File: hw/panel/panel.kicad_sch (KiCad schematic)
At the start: 37 parts, among them J1 Barrel_Jack, J2 Conn_ST_STDC14, Q1 BS170F, U1 STM32G031K8Tx, U2 RFM69HW, U3 AMS1117-3.3, U4 MCP16301Hx-xCH, Y1 32.768KHz

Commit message: panel
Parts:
- removed AE1: Antenna, RF_Antenna:NiceRF_SW868-TH13_868Mhz, symbol Device:Antenna
- removed C21, C23, C24, C25: 10uF, Capacitor_SMD:C_1206_3216Metric_Pad1.33x1.80mm_HandSolder, symbol Device:C
- removed C22: C, Capacitor_SMD:C_0805_2012Metric_Pad1.18x1.45mm_HandSolder, symbol Device:C
- removed D26: 1N4148W, Diode_SMD:D_SOD-123, symbol Diode:1N4148W
- removed D27: B140-E3, Diode_SMD:D_SMA, symbol Diode:B140-E3
- removed L1: 22uH, Inductor_SMD:L_Coilcraft_LPS4018, symbol Device:L
- removed R4: 52.3k, Resistor_SMD:R_0805_2012Metric_Pad1.20x1.40mm_HandSolder, symbol Device:R
- removed R5: 10k, Resistor_SMD:R_0805_2012Metric_Pad1.20x1.40mm_HandSolder, symbol Device:R
- removed U4: MCP16301Hx-xCH, Package_TO_SOT_SMD:SOT-23-6, symbol Regulator_Switching:MCP16301Hx-xCH
- added C11, C9: 100nF, Capacitor_SMD:C_0805_2012Metric_Pad1.18x1.45mm_HandSolder, symbol Device:C
- added C8: 4.7uF, Capacitor_SMD:C_0805_2012Metric_Pad1.18x1.45mm_HandSolder, symbol Device:C
- added J2: Conn_Coaxial, Connector_Coaxial:SMA_Amphenol_901-143_Horizontal, symbol Connector:Conn_Coaxial
- added J4: Conn_01x04_Socket, Connector_PinSocket_2.54mm:PinSocket_1x04_P2.54mm_Horizontal, symbol Connector:Conn_01x04_Socket
- added J5: Conn_01x04_Pin, Connector_PinHeader_2.54mm:PinHeader_1x04_P2.54mm_Horizontal, symbol Connector:Conn_01x04_Pin
- J1: footprint Connector_BarrelJack:BarrelJack_CUI_PJ-063AH_Horizontal -> Connector_AMASS:AMASS_XT30PW-M_1x02_P2.50mm_Horizontal
- renumbered C20 to C10, C19 to C7, H3 to H2, H2 to H3, J2 to J3, JP2 to JP1, JP26 to JP2, R2 to R1, R1 to R2, U3 to U2, U2 to U3
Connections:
- net +5V is gone; now on net +6V: C7.1, R3.1, U2.3 (VI)
- net +3V3: now also C11.1, C8.1, C9.1
- net GND: now also C11.2, C8.2, C9.2, J2.2 (Ext), J4.1 (Pin_1), J5.1 (Pin_1)
- net leds/RGB_IN: now also J5.3 (Pin_3)
- net leds/RGB_OUT: now also J4.3 (Pin_3)
- net leds1/RGB_IN: now also J4.2 (Pin_2)
- net leds1/RGB_OUT: now also J5.2 (Pin_2)
- net +6V: now reaches J1.1
- net +6V: now also J4.4 (Pin_4), J5.4 (Pin_4)
- net at U3.10 (ANA): now also J2.1 (In)
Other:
- moved on the sheet: C10, C7, J3, JP2, U2

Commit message: panel progress
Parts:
- J1: footprint Connector_AMASS:AMASS_XT30PW-M_1x02_P2.50mm_Horizontal -> Connector_Molex:Molex_Micro-Fit_3.0_43650-0200_1x02_P3.00mm_Horizontal
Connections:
- net +3V3: now also D1.2 (A); no longer R1.1
- net at U1.20 (PC6): now also R1.2; no longer D1.1 (K)
- new net: D1.1 (K), R1.1
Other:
- moved on the sheet: D1, R1

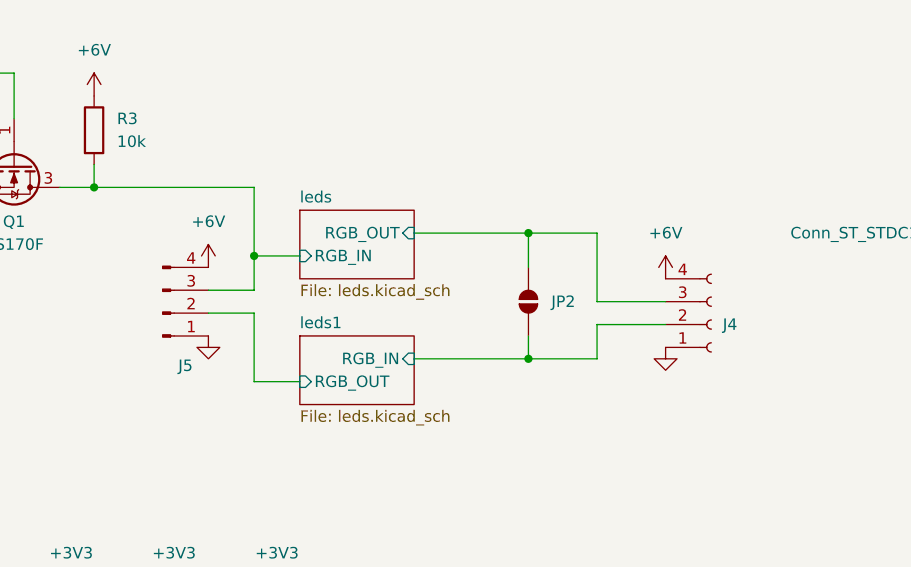
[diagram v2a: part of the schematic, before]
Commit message: extend top to 200mm
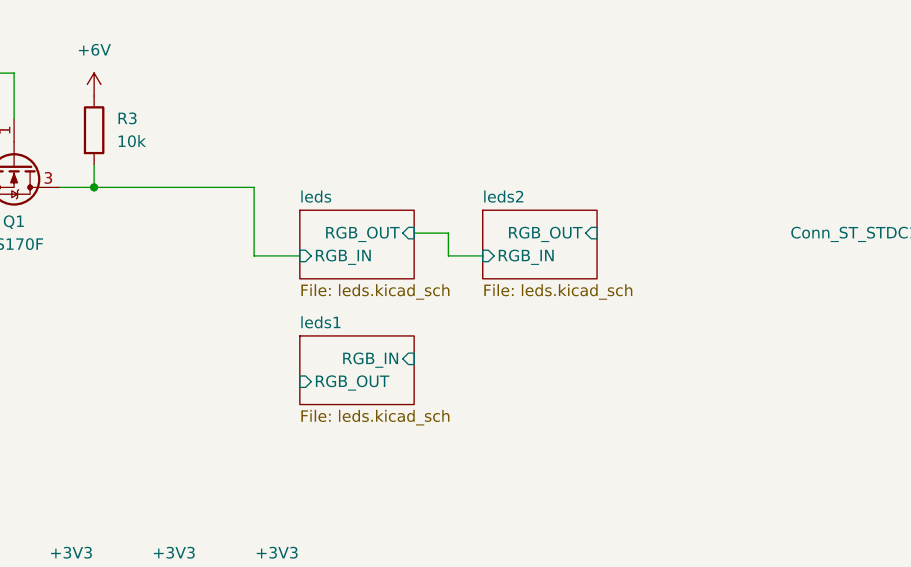
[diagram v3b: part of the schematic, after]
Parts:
- removed J4: Conn_01x04_Socket, Connector_PinSocket_2.54mm:PinSocket_1x04_P2.54mm_Horizontal, symbol Connector:Conn_01x04_Socket
- removed J5: Conn_01x04_Pin, Connector_PinHeader_2.54mm:PinHeader_1x04_P2.54mm_Horizontal, symbol Connector:Conn_01x04_Pin
- removed JP2: SolderJumper_2_Bridged, Jumper:SolderJumper-2_P1.3mm_Open_TrianglePad1.0x1.5mm, symbol Jumper:SolderJumper_2_Open
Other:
- added sheet leds2 (leds.kicad_sch)

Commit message: bot left
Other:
- sheet leds renamed led_top_left
- sheet leds1 renamed led_bot_left
- sheet leds2 renamed led_top_right
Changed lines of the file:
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@@
 			(color 0 0 0 0.0000)
 		)
-		(property "Sheetname" "leds"
+		(property "Sheetname" "led_top_left"
 			(at 173.99 60.2484 0)
 			(effects
@@
 			(color 0 0 0 0.0000)
 		)
-		(property "Sheetname" "leds1"
+		(property "Sheetname" "led_bot_left"
 			(at 173.99 74.2184 0)
 			(effects
@@
 			(project "panel"
 				(path "/75e15db9-5774-4cb3-bd4e-28bd152fa038"
-					(page "3")
+					(page "5")
 				)
 			)
@@
 			(color 0 0 0 0.0000)
 		)
-		(property "Sheetname" "leds2"
+		(property "Sheetname" "led_top_right"
 			(at 194.31 60.2484 0)
 			(effects
@@
 			(project "panel"
 				(path "/75e15db9-5774-4cb3-bd4e-28bd152fa038"
-					(page "4")
+					(page "3")
 				)
 			)

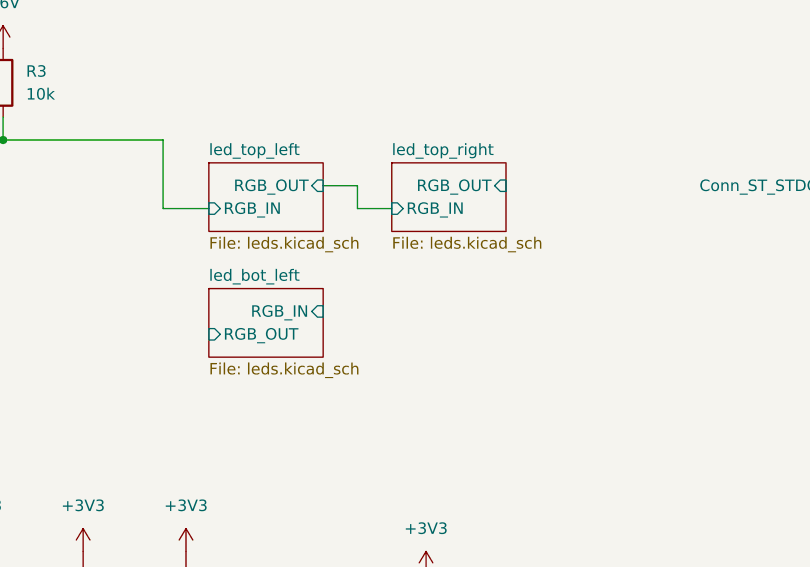
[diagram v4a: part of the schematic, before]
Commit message: Added bot right
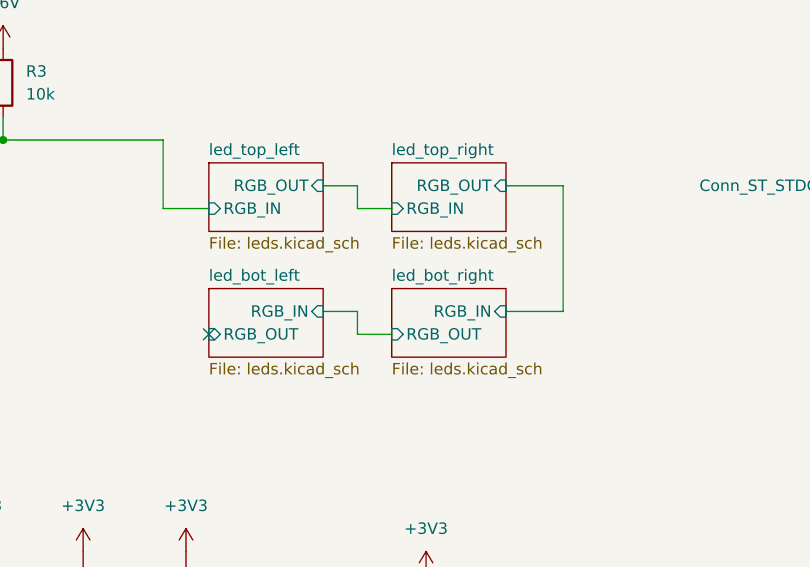
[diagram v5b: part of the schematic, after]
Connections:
- no-connect marks 23 -> 24
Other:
- added sheet led_bot_right (leds.kicad_sch)
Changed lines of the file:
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@@
 	)
 	(no_connect
+		(at 173.99 80.01)
+	)
+	(no_connect
 		(at 210.82 119.38)
 	)
@@
 	(wire
 		(pts
+			(xy 190.5 80.01) (xy 190.5 77.47)
+		)
+		(stroke
+			(width 0)
+			(type default)
+		)
+	)
+	(wire
+		(pts
 			(xy 72.39 38.1) (xy 76.2 38.1)
 		)
@@
 	(wire
 		(pts
+			(xy 194.31 80.01) (xy 190.5 80.01)
+		)
+		(stroke
+			(width 0)
+			(type default)
+		)
+	)
+	(wire
+		(pts
 			(xy 210.82 111.76) (xy 217.17 111.76)
 		)
@@
 	(wire
 		(pts
+			(xy 213.36 77.47) (xy 207.01 77.47)
+		)
+		(stroke
+			(width 0)
+			(type default)
+		)
+	)
+	(wire
+		(pts
 			(xy 102.87 149.86) (xy 102.87 147.32)
 		)
@@
 	(wire
 		(pts
+			(xy 186.69 77.47) (xy 190.5 77.47)
+		)
+		(stroke
+			(width 0)
+			(type default)
+		)
+	)
+	(wire
+		(pts
 			(xy 167.64 124.46) (xy 170.18 124.46)
 		)
@@
 	(wire
 		(pts
+			(xy 213.36 63.5) (xy 213.36 77.47)
+		)
+		(stroke
+			(width 0)
+			(type default)
+		)
+	)
+	(wire
+		(pts
 			(xy 127 151.13) (xy 127 149.86)
 		)
@@
 	(wire
 		(pts
+			(xy 207.01 63.5) (xy 213.36 63.5)
+		)
+		(stroke
+			(width 0)
+			(type default)
+		)
+	)
+	(wire
+		(pts
 			(xy 55.88 48.26) (xy 55.88 50.8)
 		)
@@
 				)
 			)
+		)
+	)
+	(sheet
+		(at 194.31 74.93)
+		(size 12.7 7.62)
+		(fields_autoplaced yes)
+		(stroke
+			(width 0.1524)
+			(type solid)
+		)
+		(fill
+			(color 0 0 0 0.0000)
+		)
+		(property "Sheetname" "led_bot_right"
+			(at 194.31 74.2184 0)
+			(effects
+				(font
+					(size 1.27 1.27)
+				)
+				(justify left bottom)
+			)
+		)
+		(property "Sheetfile" "leds.kicad_sch"
+			(at 194.31 83.1346 0)
+			(effects
+				(font
+					(size 1.27 1.27)
+				)
+				(justify left top)
+			)
+		)
+		(pin "RGB_IN" input
+			(at 207.01 77.47 0)
+			(effects
+				(font
+					(size 1.27 1.27)
+				)
+				(justify right)
+			)
+		)
+		(pin "RGB_OUT" input
+			(at 194.31 80.01 180)
+			(effects
+				(font
+					(size 1.27 1.27)
+				)
+				(justify left)
+			)
+		)
+		(instances
+			(project "panel"
+				(path "/75e15db9-5774-4cb3-bd4e-28bd152fa038"
+					(page "4")
+				)
+			)

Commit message: holes
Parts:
- added H200, H201: MountingHole, MountingHole:MountingHole_3.2mm_M3, symbol Mechanical:MountingHole
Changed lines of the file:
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@@
+	)
+	(symbol
+		(lib_id "Mechanical:MountingHole")
+		(at 257.81 22.86 0)
+		(unit 1)
+		(exclude_from_sim yes)
+		(in_bom no)
+		(on_board yes)
+		(dnp no)
+		(fields_autoplaced yes)
+		(property "Reference" "H200"
+			(at 260.35 21.5899 0)
+			(effects
+				(font
+					(size 1.27 1.27)
+				)
+				(justify left)
+				(hide yes)
+			)
+		)
+		(property "Value" "MountingHole"
+			(at 260.35 24.1299 0)
+			(effects
+				(font
+					(size 1.27 1.27)
+				)
+				(justify left)
+				(hide yes)
+			)
+		)
+		(property "Footprint" "MountingHole:MountingHole_3.2mm_M3"
+			(at 257.81 22.86 0)
+			(effects
+				(font
+					(size 1.27 1.27)
+				)
+				(hide yes)
+			)
+		)
+		(property "Datasheet" "~"
+			(at 257.81 22.86 0)
+			(effects
+				(font
+					(size 1.27 1.27)
+				)
+				(hide yes)
+			)
+		)
+		(property "Description" "Mounting Hole without connection"
+			(at 257.81 22.86 0)
+			(effects
+				(font
+					(size 1.27 1.27)
+				)
+				(hide yes)
+			)
+		)
+		(instances
+			(project "panel"
+				(path "/75e15db9-5774-4cb3-bd4e-28bd152fa038"
+					(reference "H200")
+					(unit 1)
+				)
+			)
+		)
 	)
 	(symbol
@@
 					(unit 1)
 				)
+			)
+		)
+	)
+	(symbol
+		(lib_id "Mechanical:MountingHole")
+		(at 257.81 26.67 0)
+		(unit 1)
+		(exclude_from_sim yes)
+		(in_bom no)
+		(on_board yes)
+		(dnp no)
+		(fields_autoplaced yes)
+		(property "Reference" "H201"
+			(at 260.35 25.3999 0)
+			(effects
+				(font
+					(size 1.27 1.27)
+				)
+				(justify left)
+				(hide yes)
+			)
+		)
+		(property "Value" "MountingHole"
+			(at 260.35 27.9399 0)
+			(effects
+				(font
+					(size 1.27 1.27)
+				)
+				(justify left)
+				(hide yes)
+			)
+		)
+		(property "Footprint" "MountingHole:MountingHole_3.2mm_M3"
+			(at 257.81 26.67 0)
+			(effects
+				(font
+					(size 1.27 1.27)
+				)
+				(hide yes)
+			)
+		)
+		(property "Datasheet" "~"
+			(at 257.81 26.67 0)
+			(effects
+				(font
+					(size 1.27 1.27)
+				)
+				(hide yes)
+			)
+		)
+		(property "Description" "Mounting Hole without connection"
+			(at 257.81 26.67 0)
+			(effects
+				(font
+					(size 1.27 1.27)
+				)
+				(hide yes)
+			)
+		)
+		(instances
+			(project "panel"
+				(path "/75e15db9-5774-4cb3-bd4e-28bd152fa038"
+					(reference "H201")
+					(unit 1)
+				)

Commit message: x
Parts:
- removed D1: LED, LED_SMD:LED_0805_2012Metric_Pad1.15x1.40mm_HandSolder, symbol Device:LED
- added D1: ~, panel:light_guide, symbol panel:LED_ARRAY_4
- added R4, R5, R6: 680, Resistor_SMD:R_0805_2012Metric_Pad1.20x1.40mm_HandSolder, symbol Device:R
- R1: value 100k -> 680
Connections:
- net +3V3: now also R1.2
- net GND: now also D1.1 (K), D1.3 (K), D1.5 (K), D1.7 (K)
- net LED_TX: now reaches U1.11 (PA4)
- net LED_TX: now also R4.2
- net LED_RX: now reaches U1.12 (PA5)
- net LED_RX: now also R5.2
- net LED_ERROR: now reaches U1.13 (PA6)
- net LED_ERROR: now also R6.2
- net at U1.20 (PC6): no longer R1.2
- net at R1.1: now also D1.2 (A)
- new net: D1.8 (A), R6.1
- new net: D1.4 (A), R4.1
- new net: D1.6 (A), R5.1
- no-connect marks 24 -> 21
